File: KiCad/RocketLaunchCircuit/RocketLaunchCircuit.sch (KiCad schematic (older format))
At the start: 27 parts, among them J1 Arduino_GPIO, J10 LogicConverter_BiDirectional, J11 LM2596_Module_StepDown, J12 XL6009E1_Module_StepUp, J13 ConnectorTarget3, J14 ConnectorTarget4, J15 Screw_Terminal_01x02, J16 microbit_edge_connector, J2 Arduino_Serial_And_5V, J3 MicroBit_40PinExtender, J4 ConnectorTarget1, J5 JST-PH_2P_Female, J6 Barrel_Jack_5.5mm_Male, J7 ConnectorTarget2, J8 LogicConverter_BiDirectional, J9 JST-SM_3P_Male_LedMatrix, SW1 SW_Start_Reset, SW2 SW_Player_Count, SW3 SW_Game_Mode

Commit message: Finished V1 of the circuit
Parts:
- added C5: 0.1uF, symbol Device:C
- added R5, R6, R7: 1K, symbol Device:R
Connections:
- net 5V_Arduino is gone; now on net Arduino_5V: SW2.3 (C), SW3.3 (C)
- net LedMatrixData is gone; now on net Arduino_P4: J9.2 (Pin_2)
- net StartResetSignal is gone; now on net GND: SW1.2 (B)
- net GND: now also C5.2; no longer SW1.1 (A)
- net Arduino_P4: now reaches J1.10 (Pin_10)
- net Arduino_P8: now reaches J1.6 (Pin_6)
- net Arduino_P8: now also R6.1
- net Arduino_P7: now reaches J1.7 (Pin_7)
- net Arduino_P7: now also R7.1
- net Arduino_P6: now reaches J1.8 (Pin_8)
- net Arduino_P6: now also C5.1, R5.1
- net Arduino_P5: now reaches J1.9 (Pin_9)
- net GameModeSignal: no longer names the net of SW3.2 (B)
- net GameModeSignal: now also R7.2
- net PlayerCountSignal: no longer names the net of SW2.2 (B)
- net PlayerCountSignal: now also R6.2
- net Serial_Arduino_RX_Enable_5V renamed Arduino_P2
- net Serial_MicroBit_RX_Enable_5V renamed Arduino_P3
- new net: R5.2, SW1.1 (A)
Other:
- note added: "All SwitchTarget<n> are connected to the Micro:Bit pins which have an internal pull-up resistor of 13K ohm."
- note added: "The start/reset switch is connected to the Arduino pin which has \nan internal pull-up resistor with \na value between 20K-50K ohm. (Some measured around 35K)"
- moved on the sheet: C1, C2, C3, C4, J11, J13, J14, J4, J5, J7, R1, R2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

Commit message: Change in schematic: going to use the 5V from the power supply to power the Micro:Bit and Arduino. The 5V will be provided through standard USB-A female connectors to make it possible to use a standard USB cable to power the microcontrollers.
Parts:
- removed J11: LM2596_Module_StepDown, symbol Connector_Generic:Conn_02x02_Counter_Clockwise
- removed J12: XL6009E1_Module_StepUp, symbol Connector_Generic:Conn_02x02_Counter_Clockwise
- removed J5: JST-PH_2P_Female, symbol Connector_Generic:Conn_01x02
- removed J6: Barrel_Jack_5.5mm_Male, symbol Connector:Barrel_Jack
- added J5: USB_A_PowerArduino, symbol Connector:USB_A
- added J6: USB_A_PowerMicroBit, symbol Connector:USB_A
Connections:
- net 3V3_MicroBit is gone; now on net MicroBit_3V3: J10.4a (Pin_4a)
- net 5V_PowerSupply: now also J5.1 (VBUS), J6.1 (VBUS)
- net GND: now also J5.4 (GND), J6.4 (GND)
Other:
- moved on the sheet: C5, J8, R5, R6, R7, SW1A, SW2A, SW3A

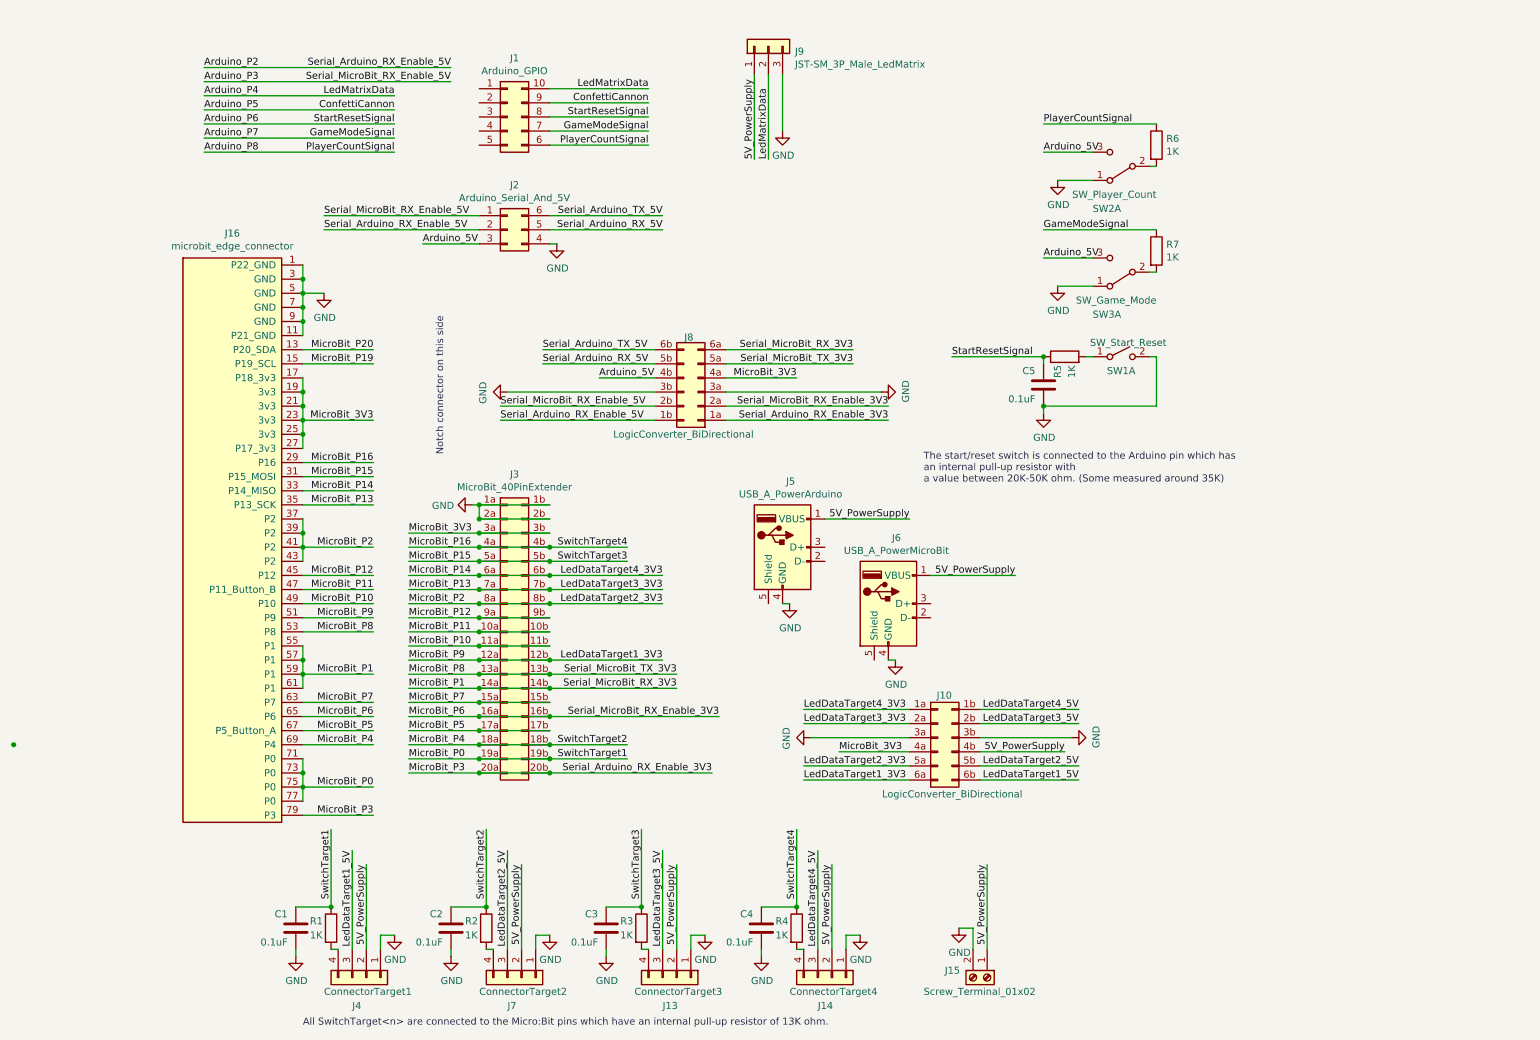
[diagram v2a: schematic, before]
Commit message: Updated the code to correspond with the circuit pins
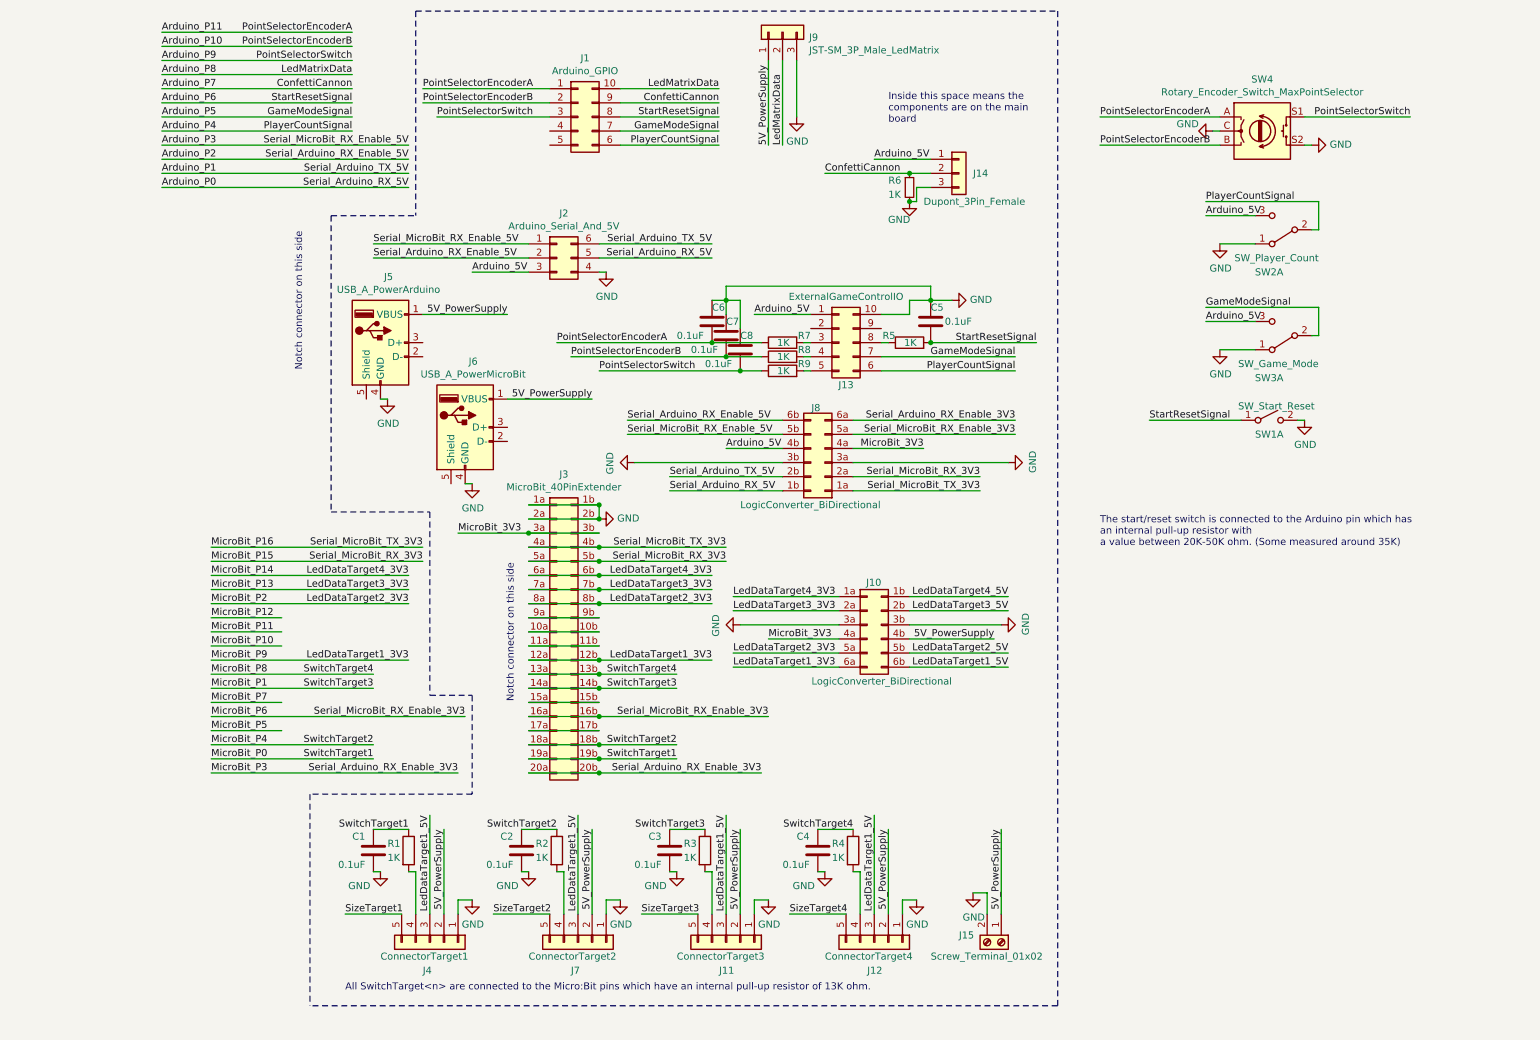
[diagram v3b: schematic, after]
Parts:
- removed J13: ConnectorTarget3, symbol Connector_Generic:Conn_01x04
- removed J14: ConnectorTarget4, symbol Connector_Generic:Conn_01x04
- removed J16: microbit_edge_connector, symbol MicroBit:microbit_edge_connector
- removed J4: ConnectorTarget1, symbol Connector_Generic:Conn_01x04
- removed J7: ConnectorTarget2, symbol Connector_Generic:Conn_01x04
- removed R6: 1K, symbol Device:R
- added C6, C7, C8: 0.1uF, symbol Device:C
- added J11: ConnectorTarget3, symbol Connector_Generic:Conn_01x05
- added J12: ConnectorTarget4, symbol Connector_Generic:Conn_01x05
- added J13: ExternalGameControlIO, symbol Connector_Generic:Conn_02x05_Counter_Clockwise
- added J14: Dupont_3Pin_Female, symbol Connector_Generic:Conn_01x03
- added J4: ConnectorTarget1, symbol Connector_Generic:Conn_01x05
- added J7: ConnectorTarget2, symbol Connector_Generic:Conn_01x05
- added R6: 1K, symbol Device:R_Small
- added R8, R9: 1K, symbol Device:R
- added SW4: Rotary_Encoder_Switch_MaxPointSelector, symbol Device:Rotary_Encoder_Switch
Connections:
- net 5V_PowerSupply: now also J11.2 (Pin_2), J12.2 (Pin_2), J4.2 (Pin_2), J7.2 (Pin_2)
- net Arduino_5V: now also J13.1 (Pin_1), J14.1 (Pin_1)
- net Arduino_P2: now also J8.6b (Pin_6b); no longer J8.1b (Pin_1b)
- net Arduino_P3: now also J8.5b (Pin_5b); no longer J8.2b (Pin_2b)
- net Arduino_P4: now also J1.6 (Pin_6), SW2.2 (B), J13.6 (Pin_6); no longer J1.10 (Pin_10), J9.2 (Pin_2)
- net Arduino_P5: now also J1.7 (Pin_7), SW3.2 (B), J13.7 (Pin_7); no longer J1.9 (Pin_9)
- net Arduino_P6: now also C5.2, R5.2, SW1.1 (A); no longer C5.1, R5.1
- net Arduino_P7: now also J1.9 (Pin_9), J14.2 (Pin_2), R6.1; no longer J1.7 (Pin_7), R7.1
- net Arduino_P8: now also J1.10 (Pin_10), J9.2 (Pin_2); no longer J1.6 (Pin_6)
- net GND: now also C5.1, C6.1, C7.1, C8.1, J11.1 (Pin_1), J12.1 (Pin_1), J13.10 (Pin_10), J14.3 (Pin_3), J4.1 (Pin_1), J7.1 (Pin_1), R6.2, SW4.C, SW4.S2; no longer C5.2
- net LedDataTarget1_5V: now also J11.3 (Pin_3), J12.3 (Pin_3), J4.3 (Pin_3), J7.3 (Pin_3)
- net MicroBit_P1: now also C3.1, R3.1; no longer J8.6a (Pin_6a)
- net MicroBit_P10: no longer J3.11a (Pin_11a), J3.11b (Pin_11b)
- net MicroBit_P11: no longer J3.10a (Pin_10a), J3.10b (Pin_10b)
- net MicroBit_P12: no longer J3.9a (Pin_9a), J3.9b (Pin_9b)
- net MicroBit_P15: now also J8.2a (Pin_2a); no longer C3.1, R3.1
- net MicroBit_P16: now also J8.1a (Pin_1a); no longer C4.1, R4.1
- net MicroBit_P3: now also J8.6a (Pin_6a); no longer J8.1a (Pin_1a)
- net MicroBit_P5: no longer J3.17a (Pin_17a), J3.17b (Pin_17b)
- net MicroBit_P6: now also J8.5a (Pin_5a); no longer J8.2a (Pin_2a)
- net MicroBit_P7: no longer J3.15a (Pin_15a), J3.15b (Pin_15b)
- net MicroBit_P8: now also C4.1, R4.1; no longer J8.5a (Pin_5a)
- net Arduino_P11: now reaches J1.1 (Pin_1)
- net Arduino_P11: now also R7.1, C6.2, SW4.A
- net Arduino_P10: now reaches J1.2 (Pin_2)
- net Arduino_P10: now also C7.2, R8.1, SW4.B
- net Arduino_P9: now reaches J1.3 (Pin_3)
- net Arduino_P9: now also C8.2, R9.1, SW4.S1
- net at R7.2: now also J13.3 (Pin_3); no longer SW3.2 (B)
- net at R1.2: now also J4.4 (Pin_4)
- net at R2.2: now also J7.4 (Pin_4)
- net at R3.2: now also J11.4 (Pin_4)
- net at R4.2: now also J12.4 (Pin_4)
- net Serial_Arduino_RX_5V renamed Arduino_P0
- net Arduino_P0: now also J8.1b (Pin_1b); no longer J8.5b (Pin_5b)
- net Serial_Arduino_TX_5V renamed Arduino_P1
- net Arduino_P1: now also J8.2b (Pin_2b); no longer J8.6b (Pin_6b)
- new net: J3.10a (Pin_10a), J3.10b (Pin_10b)
- new net: J3.11a (Pin_11a), J3.11b (Pin_11b)
- new net: J3.15a (Pin_15a), J3.15b (Pin_15b)
- new net: J3.17a (Pin_17a), J3.17b (Pin_17b)
- new net: J3.9a (Pin_9a), J3.9b (Pin_9b)
- new net: J13.4 (Pin_4), R8.2
- new net: J13.5 (Pin_5), R9.2
- new net: J13.8 (Pin_8), R5.1
- new net SizeTarget1: J4.5 (Pin_5)
- new net SizeTarget2: J7.5 (Pin_5)
- new net SizeTarget3: J11.5 (Pin_5)
- new net SizeTarget4: J12.5 (Pin_5)
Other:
- note added: "Inside this space means the\ncomponents are on the main\nboard"
- moved on the sheet: C5, J1, J10, J15, J2, J3, J5, J6, J8, J9, R5, SW1A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
